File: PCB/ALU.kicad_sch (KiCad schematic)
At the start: 30 parts, among them U10 74LS08, U11 74LS02, U12 74LS173, U13 74LS283, U14 74LS283, U15 74LS86, U16 74LS86, U17 74LS245

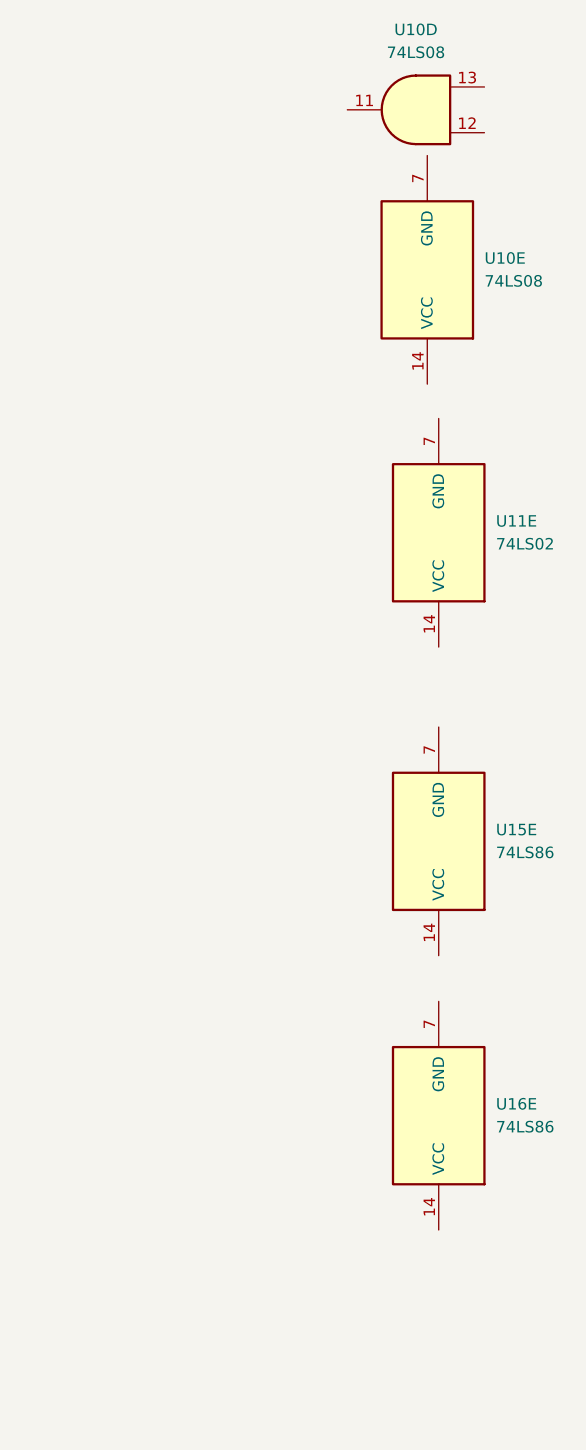
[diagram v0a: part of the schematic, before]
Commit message: Cleaned up the schematic and got started on assigning all the footprints to the symbols
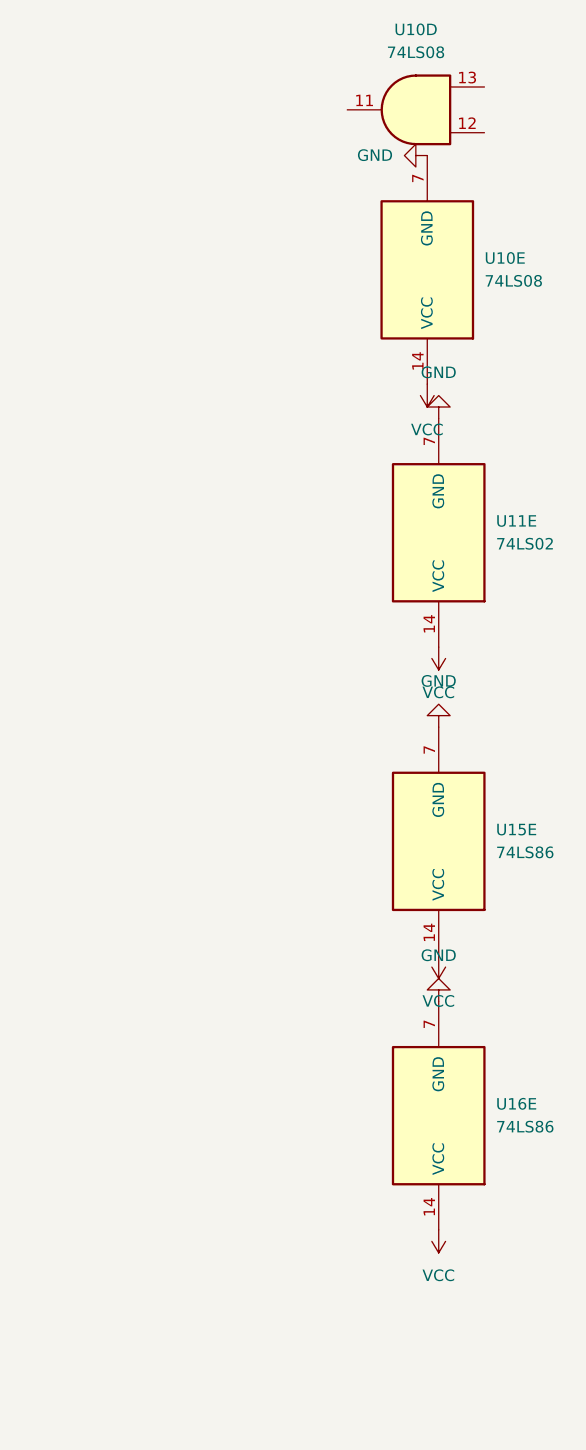
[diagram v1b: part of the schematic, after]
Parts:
- C10, C9: footprint (none) -> Capacitor_THT:C_Radial_D5.0mm_H5.0mm_P2.00mm
- D10: footprint (none) -> LED_THT:LED_D1.8mm_W1.8mm_H2.4mm_Horizontal_O1.27mm_Z1.6mm
- R10, R11, R12, R13, R14, R15, R16, R17, R8, R9: footprint (none) -> Resistor_THT:R_Axial_DIN0207_L6.3mm_D2.5mm_P7.62mm_Horizontal
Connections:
- net GND: now also U10.7 (GND), U11.7 (GND), U15.7 (GND), U16.7 (GND)
- net VCC: now also U10.14 (VCC), U11.14 (VCC), U15.14 (VCC), U16.14 (VCC)

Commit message: added more models to work with on my pcb
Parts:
- D10, D14: value LED -> GREEN; footprint LED_THT:LED_D1.8mm_W1.8mm_H2.4mm_Horizontal_O1.27mm_Z1.6mm -> LED_THT:LED_D3.0mm
- D11, D12, D13, D15, D16, D17, D18, D19: value LED -> RED; footprint LED_THT:LED_D1.8mm_W1.8mm_H2.4mm_Horizontal_O1.27mm_Z1.6mm -> LED_THT:LED_D3.0mm
- U11, U15, U16: footprint (none) -> footprints:N14
- U17: footprint (none) -> Custom:DIP254P762X508-20
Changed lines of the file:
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@@
 			)
 		)
-		(property "Footprint" ""
+		(property "Footprint" "footprints:N14"
 			(at 283.21 113.03 0)
 			(effects
@@
 			)
 		)
-		(property "Footprint" ""
+		(property "Footprint" "footprints:N14"
 			(at 373.38 111.76 0)
 			(effects
@@
 			)
 		)
-		(property "Value" "LED"
+		(property "Value" "GREEN"
 			(at 67.6275 119.38 0)
 			(effects
@@
 			)
 		)
-		(property "Footprint" "LED_THT:LED_D1.8mm_W1.8mm_H2.4mm_Horizontal_O1.27mm_Z1.6mm"
+		(property "Footprint" "LED_THT:LED_D3.0mm"
 			(at 66.04 115.57 0)
 			(effects
@@
 			)
 		)
-		(property "Footprint" ""
+		(property "Footprint" "footprints:N14"
 			(at 139.7 210.82 0)
 			(effects
@@
 			)
 		)
-		(property "Footprint" ""
+		(property "Footprint" "footprints:N14"
 			(at 139.7 184.15 0)
 			(effects
@@
 			)
 		)
-		(property "Footprint" ""
+		(property "Footprint" "footprints:N14"
 			(at 283.21 97.79 0)
 			(effects
@@
 			)
 		)
-		(property "Footprint" ""
+		(property "Footprint" "footprints:N14"
 			(at 283.21 140.97 0)
 			(effects
@@
 			)
 		)
-		(property "Footprint" ""
+		(property "Footprint" "footprints:N14"
 			(at 373.38 77.47 0)
 			(effects
@@
 			)
 		)
-		(property "Value" "LED"
+		(property "Value" "RED"
 			(at 115.316 141.986 0)
 			(effects
@@
 			)
 		)
-		(property "Footprint" "LED_THT:LED_D1.8mm_W1.8mm_H2.4mm_Horizontal_O1.27mm_Z1.6mm"
+		(property "Footprint" "LED_THT:LED_D3.0mm"
 			(at 116.84 144.78 0)
 			(effects
@@
 			)
 		)
-		(property "Value" "LED"
+		(property "Value" "GREEN"
 			(at 67.6275 109.22 0)
 			(effects
@@
 			)
 		)
-		(property "Footprint" "LED_THT:LED_D1.8mm_W1.8mm_H2.4mm_Horizontal_O1.27mm_Z1.6mm"
+		(property "Footprint" "LED_THT:LED_D3.0mm"
 			(at 66.04 105.41 0)
 			(effects
@@
 			)
 		)
-		(property "Footprint" ""
+		(property "Footprint" "footprints:N14"
 			(at 283.21 66.04 0)
 			(effects
@@
 			)
 		)
-		(property "Value" "LED"
+		(property "Value" "RED"
 			(at 115.062 151.13 0)
 			(effects
@@
 			)
 		)
-		(property "Footprint" "LED_THT:LED_D1.8mm_W1.8mm_H2.4mm_Horizontal_O1.27mm_Z1.6mm"
+		(property "Footprint" "LED_THT:LED_D3.0mm"
 			(at 116.84 153.67 0)
 			(effects
@@
 			)
 		)
-		(property "Value" "LED"
+		(property "Value" "RED"
 			(at 115.062 97.79 0)
 			(effects
@@
 			)
 		)
-		(property "Footprint" "LED_THT:LED_D1.8mm_W1.8mm_H2.4mm_Horizontal_O1.27mm_Z1.6mm"
+		(property "Footprint" "LED_THT:LED_D3.0mm"
 			(at 116.84 100.33 0)
 			(effects
@@
 			)
 		)
-		(property "Value" "LED"
+		(property "Value" "RED"
 			(at 115.062 124.714 0)
 			(effects
@@
 			)
 		)
-		(property "Footprint" "LED_THT:LED_D1.8mm_W1.8mm_H2.4mm_Horizontal_O1.27mm_Z1.6mm"
+		(property "Footprint" "LED_THT:LED_D3.0mm"
 			(at 116.84 127 0)
 			(effects
@@
 			)
 		)
-		(property "Footprint" ""
+		(property "Footprint" "Custom:DIP254P762X508-20"
 			(at 181.61 82.55 0)
 			(effects
@@
 			)
 		)
-		(property "Value" "LED"
+		(property "Value" "RED"
 			(at 115.316 133.35 0)
 			(effects
@@
 			)
 		)
-		(property "Footprint" "LED_THT:LED_D1.8mm_W1.8mm_H2.4mm_Horizontal_O1.27mm_Z1.6mm"
+		(property "Footprint" "LED_THT:LED_D3.0mm"
 			(at 116.84 135.89 0)
 			(effects
@@
 			)
 		)
-		(property "Footprint" ""
+		(property "Footprint" "footprints:N14"
 			(at 373.38 142.24 0)
 			(effects
@@
 			)
 		)
-		(property "Footprint" ""
+		(property "Footprint" "footprints:N14"
 			(at 139.7 170.18 0)
 			(effects
@@
 			)
 		)
-		(property "Value" "LED"
+		(property "Value" "RED"
 			(at 115.316 160.274 0)
 			(effects
@@
 			)
 		)
-		(property "Footprint" "LED_THT:LED_D1.8mm_W1.8mm_H2.4mm_Horizontal_O1.27mm_Z1.6mm"
+		(property "Footprint" "LED_THT:LED_D3.0mm"
 			(at 116.84 162.56 0)
 			(effects
@@
 			)
 		)
-		(property "Footprint" ""
+		(property "Footprint" "footprints:N14"
 			(at 283.21 82.55 0)
 			(effects
@@
 			)
 		)
-		(property "Footprint" ""
+		(property "Footprint" "footprints:N14"
 			(at 283.21 154.94 0)
 			(effects
@@
 			)
 		)
-		(property "Value" "LED"
+		(property "Value" "RED"
 			(at 115.316 115.57 0)
 			(effects
@@
 			)
 		)
-		(property "Footprint" "LED_THT:LED_D1.8mm_W1.8mm_H2.4mm_Horizontal_O1.27mm_Z1.6mm"
+		(property "Footprint" "LED_THT:LED_D3.0mm"
 			(at 116.84 118.11 0)
 			(effects
@@
 			)
 		)
-		(property "Value" "LED"
+		(property "Value" "RED"
 			(at 115.062 106.68 0)
 			(effects
@@
 			)
 		)
-		(property "Footprint" "LED_THT:LED_D1.8mm_W1.8mm_H2.4mm_Horizontal_O1.27mm_Z1.6mm"
+		(property "Footprint" "LED_THT:LED_D3.0mm"
 			(at 116.84 109.22 0)
 			(effects
@@
 			)
 		)
-		(property "Footprint" ""
+		(property "Footprint" "footprints:N14"
 			(at 283.21 168.91 0)
 			(effects
@@
 			)
 		)
-		(property "Footprint" ""
+		(property "Footprint" "footprints:N14"
 			(at 283.21 127 0)
 			(effects
@@
 			)
 		)
-		(property "Footprint" ""
+		(property "Footprint" "footprints:N14"
 			(at 139.7 196.85 0)
 			(effects

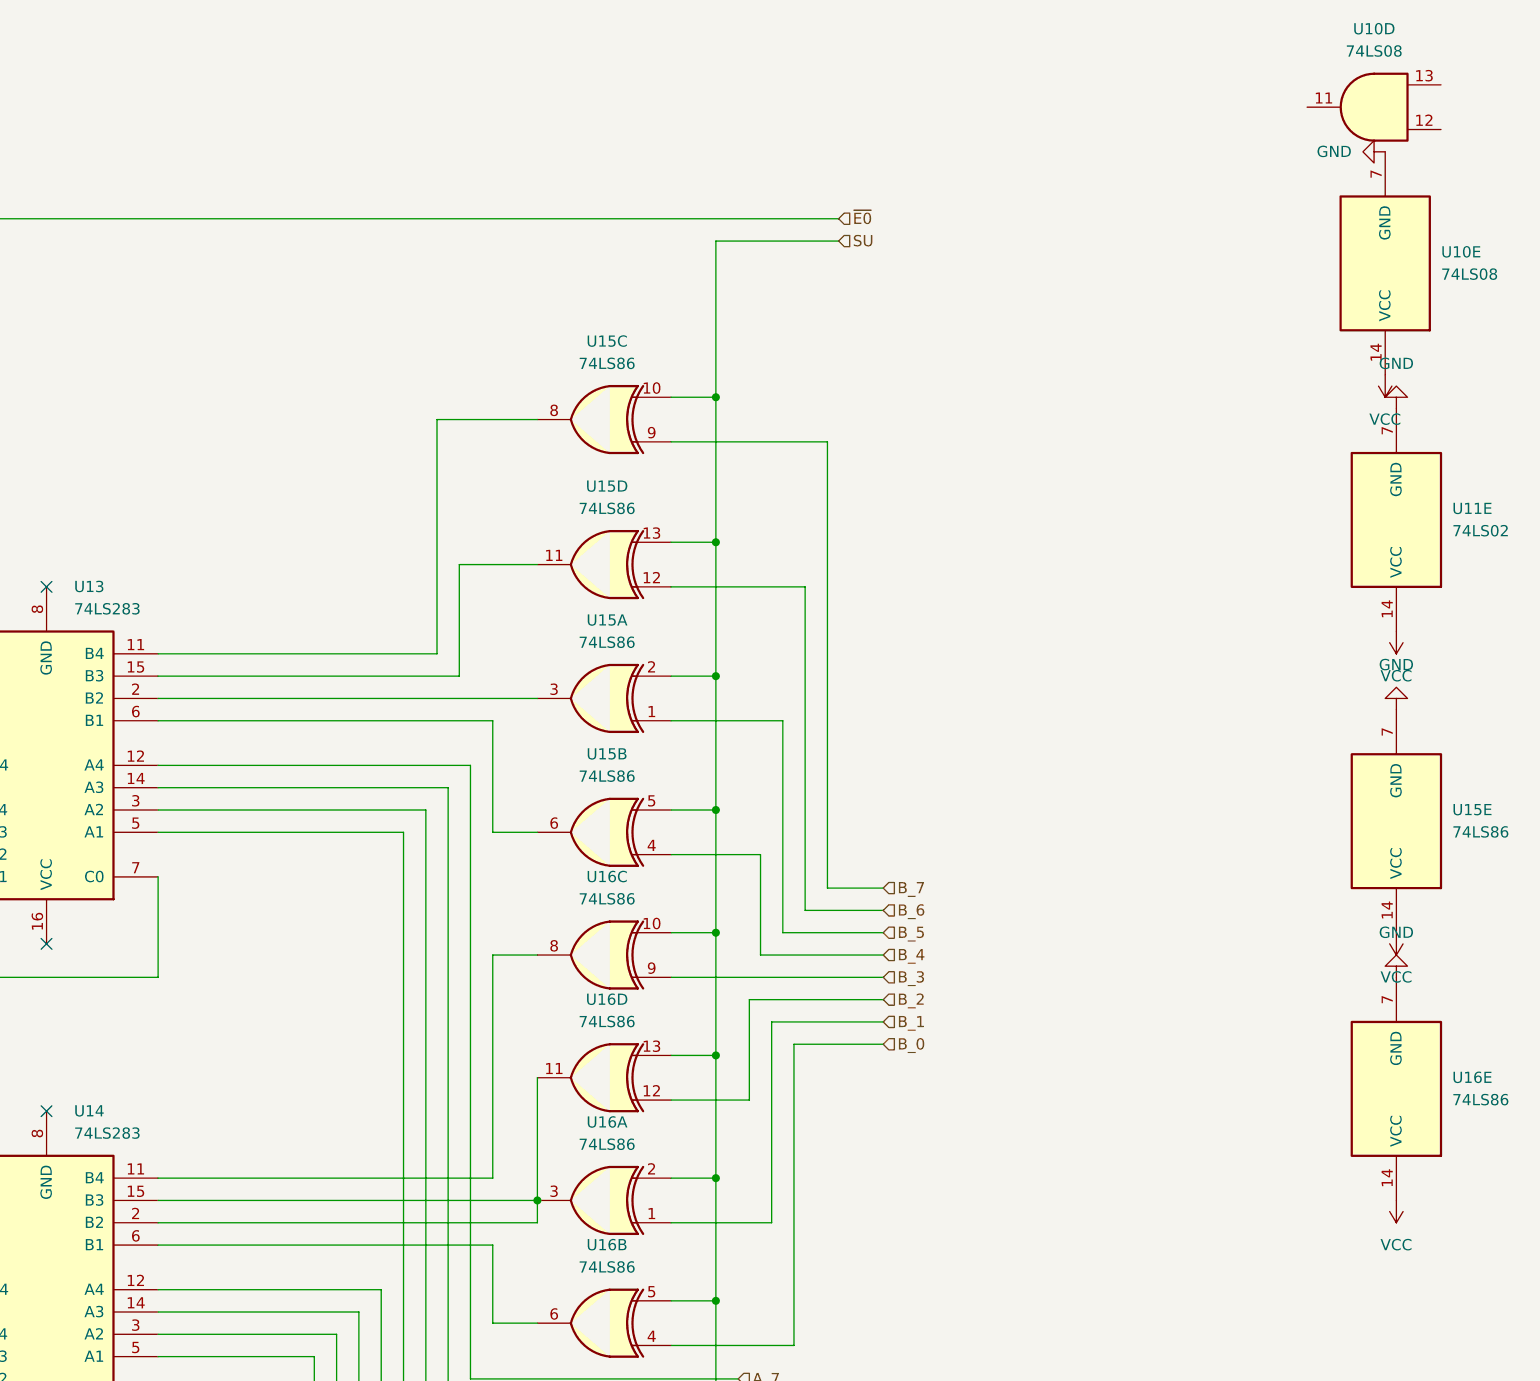
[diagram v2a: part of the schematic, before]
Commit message: Fixed a bunch of ERC errors so know there is only one remaining.
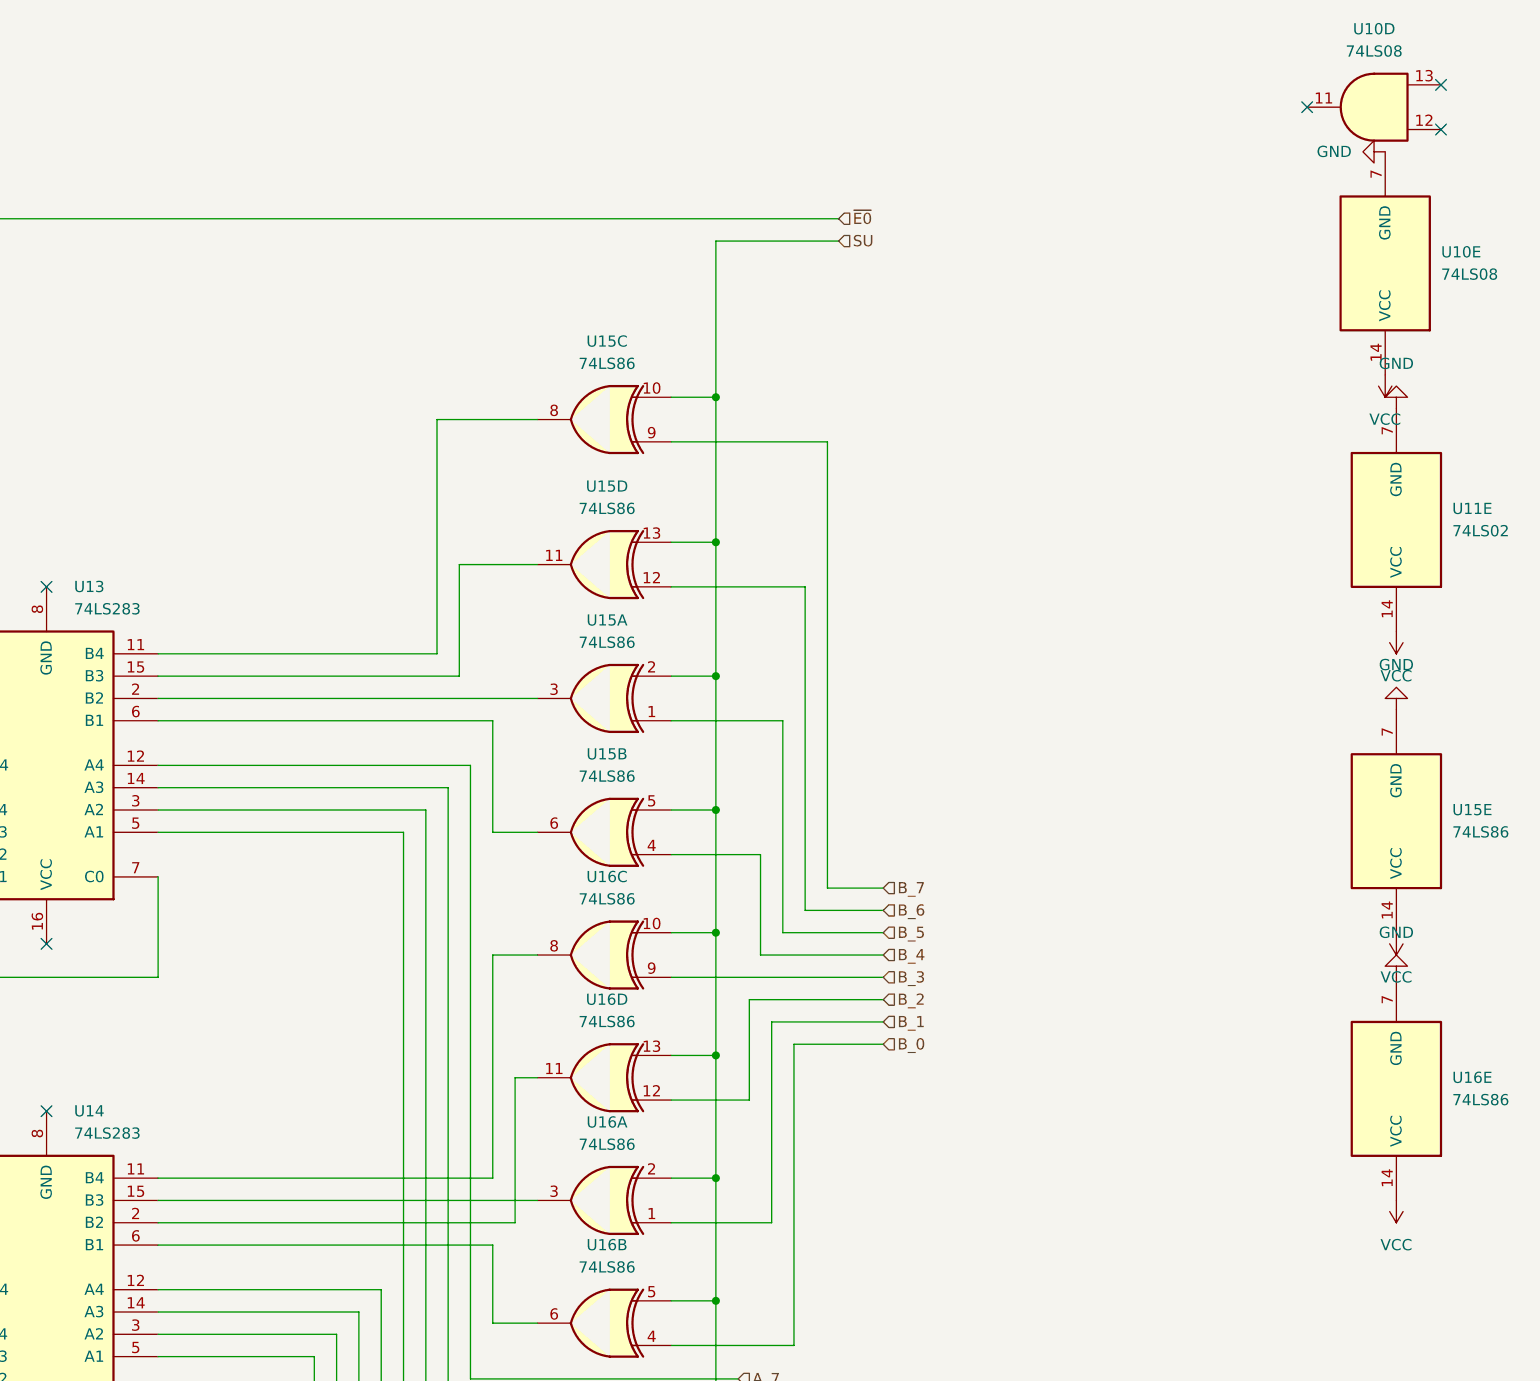
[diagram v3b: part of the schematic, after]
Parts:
- U16: footprint footprints:N14 -> Package_DIP:DIP-14_W7.62mm
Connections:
- net at U14.2 (B2), U16.11: no longer U14.15 (B3), U16.3
- new net: U14.15 (B3), U16.3
- no-connect marks 12 -> 15
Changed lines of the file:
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@@
 	)
 	(junction
-		(at 275.59 154.94)
-		(diameter 0)
-		(color 0 0 0 0)
-	)
-	(junction
 		(at 168.91 100.33)
 		(diameter 0)
@@
 	)
 	(no_connect
+		(at 378.46 27.94)
+	)
+	(no_connect
+		(at 378.46 33.02)
+	)
+	(no_connect
+		(at 363.22 30.48)
+	)
+	(no_connect
 		(at 55.88 121.92)
 	)
@@
 	(wire
 		(pts
+			(xy 232.41 157.48) (xy 273.05 157.48)
+		)
+		(stroke
+			(width 0)
+			(type default)
+		)
+	)
+	(wire
+		(pts
 			(xy 76.2 147.32) (xy 76.2 157.48)
 		)
@@
 	(wire
 		(pts
+			(xy 273.05 157.48) (xy 273.05 140.97)
+		)
+		(stroke
+			(width 0)
+			(type default)
+		)
+	)
+	(wire
+		(pts
 			(xy 232.41 113.03) (xy 260.35 113.03)
 		)
@@
 	(wire
 		(pts
-			(xy 275.59 157.48) (xy 275.59 154.94)
-		)
-		(stroke
-			(width 0)
-			(type default)
-		)
-	)
-	(wire
-		(pts
 			(xy 97.79 165.1) (xy 97.79 162.56)
 		)
@@
 	(wire
 		(pts
+			(xy 273.05 140.97) (xy 275.59 140.97)
+		)
+		(stroke
+			(width 0)
+			(type default)
+		)
+	)
+	(wire
+		(pts
 			(xy 173.99 118.11) (xy 173.99 181.61)
 		)
@@
 	(wire
 		(pts
-			(xy 275.59 154.94) (xy 275.59 140.97)
-		)
-		(stroke
-			(width 0)
-			(type default)
-		)
-	)
-	(wire
-		(pts
 			(xy 262.89 110.49) (xy 262.89 180.34)
 		)
@@
 	(wire
 		(pts
-			(xy 232.41 157.48) (xy 275.59 157.48)
-		)
-		(stroke
-			(width 0)
-			(type default)
-		)
-	)
-	(wire
-		(pts
 			(xy 115.57 196.85) (xy 132.08 196.85)
 		)
@@
 			)
 		)
-		(property "Footprint" "footprints:N14"
+		(property "Footprint" "Package_DIP:DIP-14_W7.62mm"
 			(at 283.21 140.97 0)
 			(effects
@@
 			)
 		)
-		(property "Footprint" "footprints:N14"
+		(property "Footprint" "Package_DIP:DIP-14_W7.62mm"
 			(at 373.38 142.24 0)
 			(effects
@@
 			)
 		)
-		(property "Footprint" "footprints:N14"
+		(property "Footprint" "Package_DIP:DIP-14_W7.62mm"
 			(at 283.21 154.94 0)
 			(effects
@@
 			)
 		)
-		(property "Footprint" "footprints:N14"
+		(property "Footprint" "Package_DIP:DIP-14_W7.62mm"
 			(at 283.21 168.91 0)
 			(effects
@@
 			)
 		)
-		(property "Footprint" "footprints:N14"
+		(property "Footprint" "Package_DIP:DIP-14_W7.62mm"
 			(at 283.21 127 0)
 			(effects
